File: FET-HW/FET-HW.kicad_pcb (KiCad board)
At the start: 4 copper layers, 60 x 95 mm, 24 parts, among them J1 Pins_2.54_1x12, Q1 IRF7769L1TRPBF, Q10 IRF7769L1TRPBF, Q11 IRF7769L1TRPBF, Q12 IRF7769L1TRPBF, Q13 IRF7769L1TRPBF, Q14 IRF7769L1TRPBF, Q15 IRF7769L1TRPBF, Q16 IRF7769L1TRPBF, Q17 IRF7769L1TRPBF, Q18 IRF7769L1TRPBF, Q2 IRF7769L1TRPBF, Q3 IRF7769L1TRPBF, Q4 IRF7769L1TRPBF, Q5 IRF7769L1TRPBF, Q6 IRF7769L1TRPBF, Q7 IRF7769L1TRPBF, Q8 IRF7769L1TRPBF, Q9 IRF7769L1TRPBF

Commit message: Add in some capacitance
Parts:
- added C1: 4u7,100v, C_Capacitor:C_1206, F.Cu at (56.9, 111.9)
- added C10: 4u7,100v, C_Capacitor:C_1206, F.Cu at (57.0, 76.7)
- added C11: 4u7,100v, C_Capacitor:C_1206, F.Cu at (57.0, 74.4)
- added C12: 4u7,100v, C_Capacitor:C_1206, F.Cu at (57.0, 72.1)
- added C13: 4u7,100v, C_Capacitor:C_1206, F.Cu at (57.0, 69.8)
- added C14: 4u7,100v, C_Capacitor:C_1206, F.Cu at (57.0, 67.5)
- added C15: 4u7,100v, C_Capacitor:C_1206, F.Cu at (72.2, 132.7)
- added C16: 4u7,100v, C_Capacitor:C_1206, F.Cu at (69.9, 132.7)
- added C17: 4u7,100v, C_Capacitor:C_1206, F.Cu at (67.6, 132.7)
- added C18: 4u7,100v, C_Capacitor:C_1206, F.Cu at (65.3, 132.7)
- added C2: 4u7,100v, C_Capacitor:C_1206, F.Cu at (56.9, 114.2)
- added C3: 4u7,100v, C_Capacitor:C_1206, F.Cu at (56.9, 116.5)
- added C4: 4u7,100v, C_Capacitor:C_1206, F.Cu at (56.9, 118.8)
- added C5: 4u7,100v, C_Capacitor:C_1206, F.Cu at (76.8, 132.7)
- added C6: 4u7,100v, C_Capacitor:C_1206, F.Cu at (74.5, 132.7)
- added C7: 4u7,100v, C_Capacitor:C_1206, F.Cu at (57.0, 83.6)
- added C8: 4u7,100v, C_Capacitor:C_1206, F.Cu at (57.0, 81.3)
- added C9: 4u7,100v, C_Capacitor:C_1206, F.Cu at (57.0, 79.0)
- added kibuzzard-64044190: G***, kibuzzard-64044190, F.Cu at (88.0, 60.2)
- added kibuzzard-6404419B: G***, kibuzzard-6404419B, F.Cu at (88.2, 80.1)
- added kibuzzard-640441A5: G***, kibuzzard-640441A5, F.Cu at (88.3, 100.5)
- added kibuzzard-640441AC: G***, kibuzzard-640441AC, F.Cu at (88.3, 120.1)
- added kibuzzard-640441B5: G***, kibuzzard-640441B5, F.Cu at (88.4, 140.2)
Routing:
- net GND: vias 283 -> 280
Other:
- board text added: "BESC-FET v1.0 Mar 23"

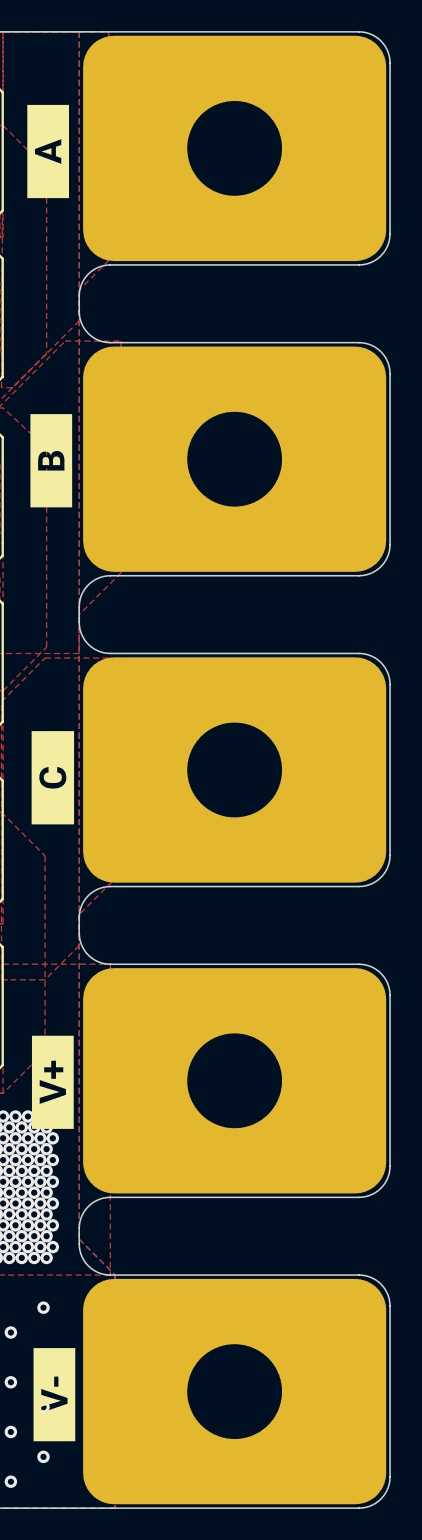
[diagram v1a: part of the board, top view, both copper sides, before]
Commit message: Put vias on fingers
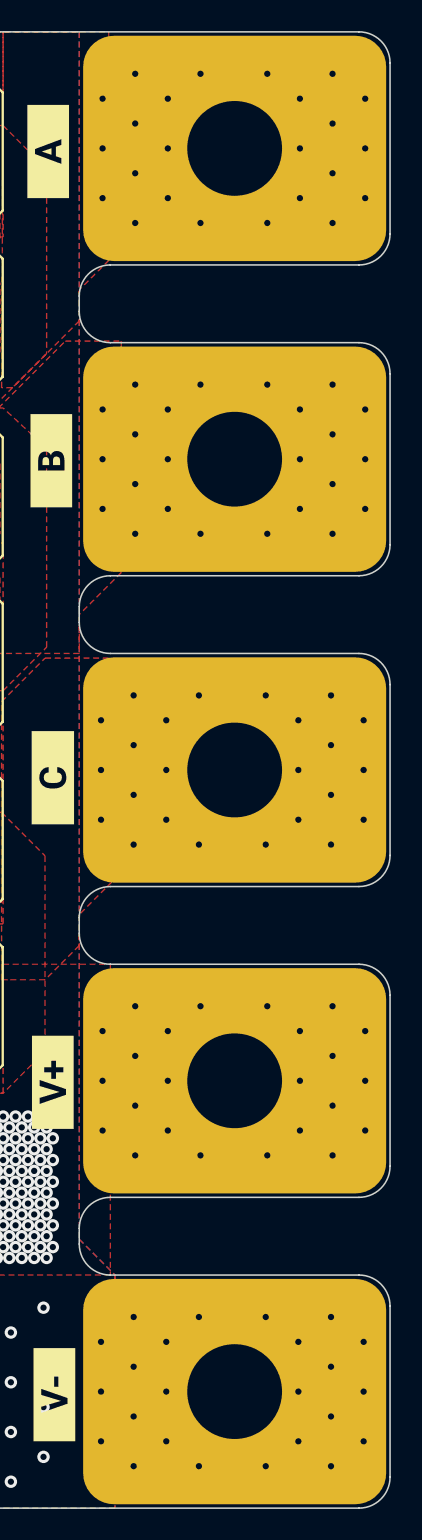
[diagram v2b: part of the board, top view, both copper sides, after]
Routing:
- net GND: vias 280 -> 304
- net /PHASE_C: vias 2 -> 26
- net /PHASE_B: vias 1 -> 25
- net /PHASE_A: vias 2 -> 26
- net +BATT: vias 261 -> 285

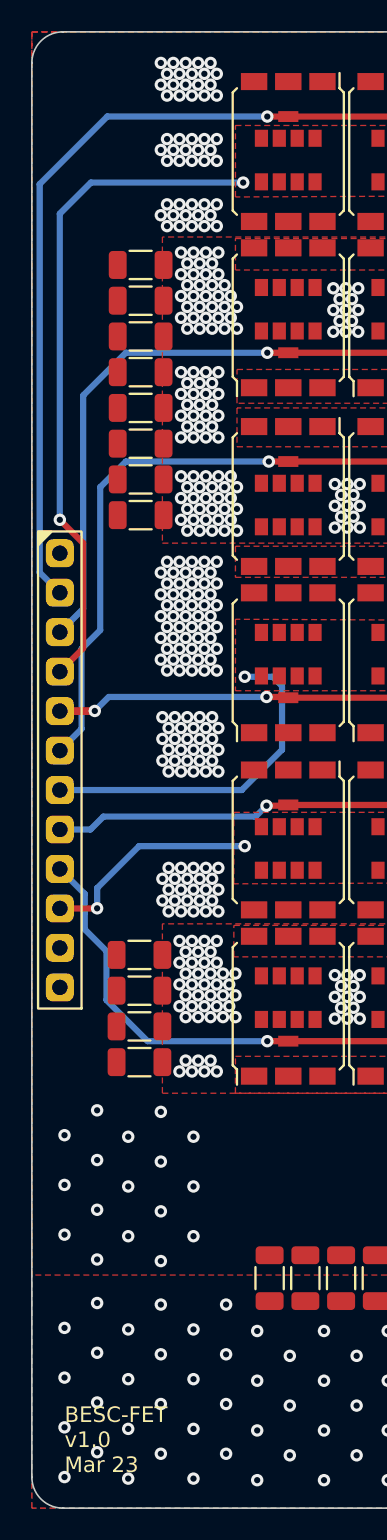
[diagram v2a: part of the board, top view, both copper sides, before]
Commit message: Add TH capacitors
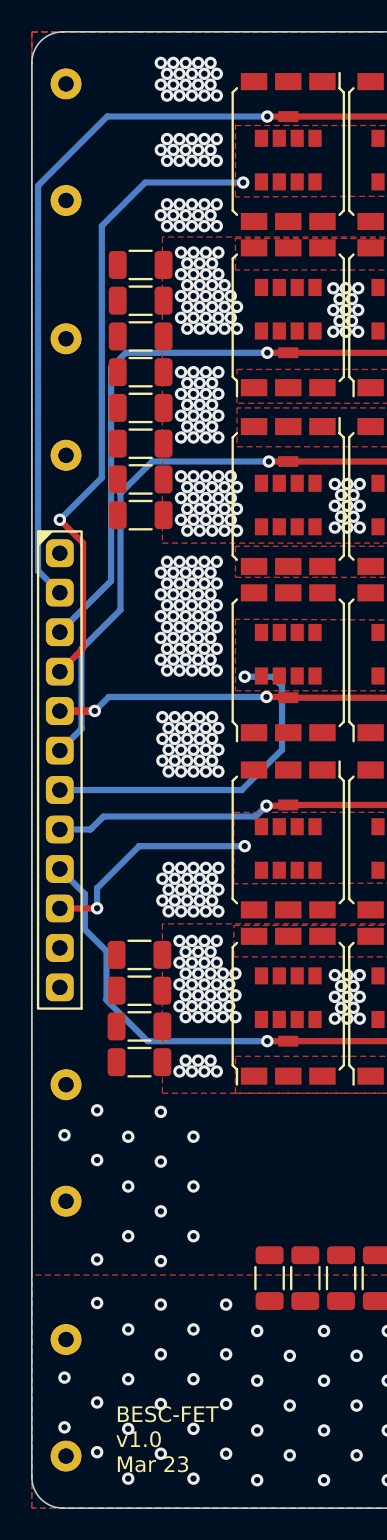
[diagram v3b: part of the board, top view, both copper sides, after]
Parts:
- added C19: 470u,100v, Capacitor_THT:C_Radial_D16.0mm_H25.0mm_P7.50mm, B.Cu at (52.2, 59.6)
- added C20: 470u,100v, Capacitor_THT:C_Radial_D16.0mm_H25.0mm_P7.50mm, B.Cu at (52.2, 76.0)
- added C21: 470u,100v, Capacitor_THT:C_Radial_D16.0mm_H25.0mm_P7.50mm, B.Cu at (52.2, 124.0)
- added C22: 470u,100v, Capacitor_THT:C_Radial_D16.0mm_H25.0mm_P7.50mm, B.Cu at (52.2, 140.4)
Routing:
- net /PHASE_A: track 43.3 -> 41.3 mm
- net /GATE_BL: track 45.8 -> 44.8 mm
- net GND: vias 304 -> 301
- net +BATT: vias 285 -> 282
